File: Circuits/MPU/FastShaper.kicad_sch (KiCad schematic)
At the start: 34 parts, among them U20 ADA4805-2ARMZ, U21 ADA4805-2ARMZ

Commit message: revert cap changes from sim. Don't trust it...
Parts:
- C89: value 200pF -> 360pF
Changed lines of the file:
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@@
 			)
 		)
-		(property "Value" "200pF"
+		(property "Value" "360pF"
 			(at 190.5 127 90)
 			(effects

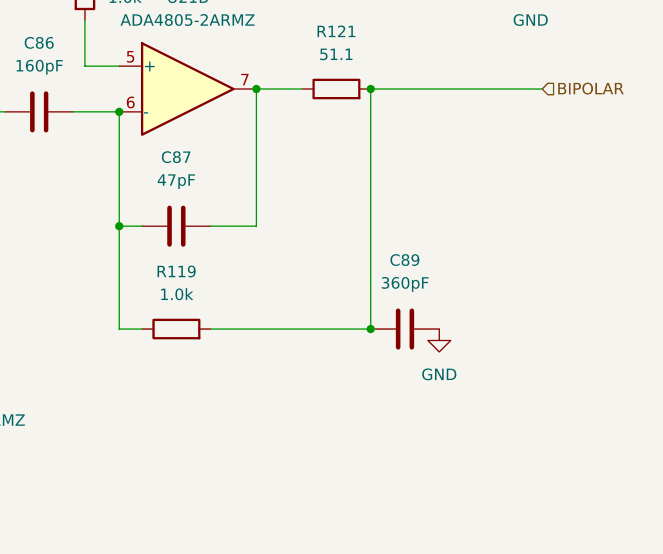
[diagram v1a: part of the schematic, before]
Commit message: tweak shaper caps based on sim
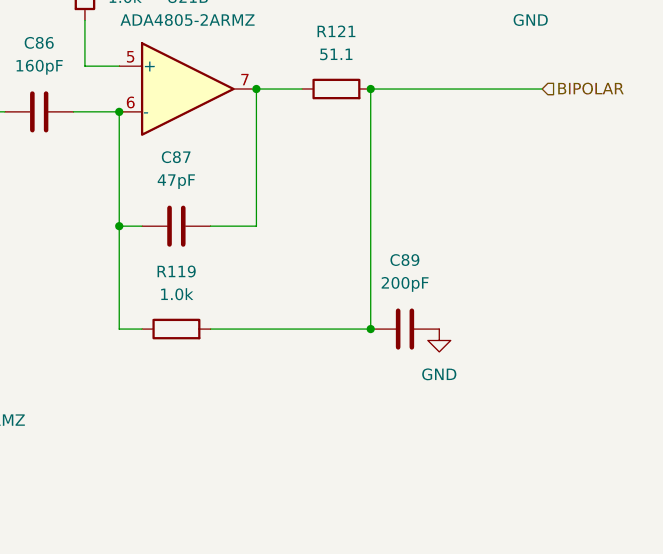
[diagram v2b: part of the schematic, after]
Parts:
- C89: value 360pF -> 200pF
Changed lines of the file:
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@@
 			)
 		)
-		(property "Value" "360pF"
+		(property "Value" "200pF"
 			(at 190.5 127 90)
 			(effects
